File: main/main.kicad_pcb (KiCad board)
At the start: 2 copper layers, 28 parts, among them J1 Conn_01x10_Female, J2 USB_B, J3 AVR-ISP-6, J4 Micro_SD_Card, Q1 2N7002, Q2 BSS84, SW1 SW_Push, U1 ATmega1284P-PU, U2 AMS1117, U3 MCP2221A-I_SL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

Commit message: laid out pcb
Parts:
- added C8: 1u, Capacitor_SMD:C_1206_3216Metric, F.Cu at (101.2, 123.8)
- added C9: 1u, Capacitor_SMD:C_1206_3216Metric, F.Cu at (84.2, 123.2)
- U1: footprint Package_DIP:DIP-40_W15.24mm -> Package_QFP:TQFP-44_10x10mm_P0.8mm
- moved R6 96.3 mm to (81.4, 113.2), turned to 180 degrees
- moved J3 86.5 mm to (64.5, 86.0), turned to 90 degrees
- moved R7 84.5 mm to (84.2, 107.4), turned to 270 degrees
- moved U4 84.3 mm to (88.8, 90.0), turned to 180 degrees
- moved U2 81.3 mm to (89.8, 110.7), turned to 90 degrees
- moved J2 71.2 mm to (74.5, 120.8), turned to 180 degrees
- moved J4 70.1 mm to (66.8, 101.0), turned to 270 degrees
- moved R5 69.8 mm to (77.8, 95.0)
- moved C5 69.6 mm to (96.3, 107.5)
- moved R4 63.1 mm to (96.6, 85.8), turned to 180 degrees
- moved R3 62.6 mm to (103.1, 87.0)
- moved R8 60.0 mm to (81.0, 107.4), turned to 270 degrees
- moved U5 59.9 mm to (88.8, 98.9), turned to 180 degrees
- moved C7 57.8 mm to (80.8, 123.2), turned to 90 degrees
- moved U3 57.2 mm to (98.7, 115.7), turned to 180 degrees
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- renumbered SW1 to Reset
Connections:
- net Net-(J2-Pad2) renamed D-
- net Net-(J2-Pad3) renamed D+
- U4 pad 10: Net-(J3-Pad1) -> Net-(J3-Pad4)
- U4 pad 11: Net-(J3-Pad4) -> Net-(J3-Pad1)
- U4 pad 4: MOSI -> MISO
- U4 pad 5: MISO -> MOSI
- U5 pad 10: SD_MISO -> SD_MOSI
- U5 pad 11: SD_MOSI -> SD_MISO
- U5 pad 4: MOSI -> MISO
- U5 pad 5: MISO -> MOSI
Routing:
- net +3V3: track 0.00 -> 80.6 mm
- net RST: track 0.00 -> 75.9 mm
- net GND: track 0.00 -> 48.8 mm, vias 0 -> 17
- net SD_CS: track 0.00 -> 33.3 mm, vias 0 -> 3
- net Net-(J3-Pad1): track 0.00 -> 27.3 mm
- net Net-(Q2-Pad1): track 0.00 -> 26.5 mm
- net +5V: track 0.00 -> 24.7 mm, vias 0 -> 10
- net D+: track 0.00 -> 24.7 mm
- net SD_MOSI: track 0.00 -> 22.6 mm, vias 0 -> 2
- net Net-(J3-Pad4): track 0.00 -> 22.6 mm
- net SD_MISO: track 0.00 -> 22.5 mm, vias 0 -> 3
- net D-: track 0.00 -> 22.3 mm
- net CS: track 0.00 -> 22.1 mm, vias 0 -> 2
- net Net-(J3-Pad3): track 0.00 -> 21.7 mm
- net MOSI: track 0.00 -> 21.7 mm, vias 0 -> 2
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- added copper zone on VCC.Cu, net +5V
- added copper zone on GND.Cu, net GND
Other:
- board outline added: 70 x 57.5 mm
- copper layers 2 -> 4
- board text added: "3.3V ISP AVR"
- board text added: "Snug User Board V1"

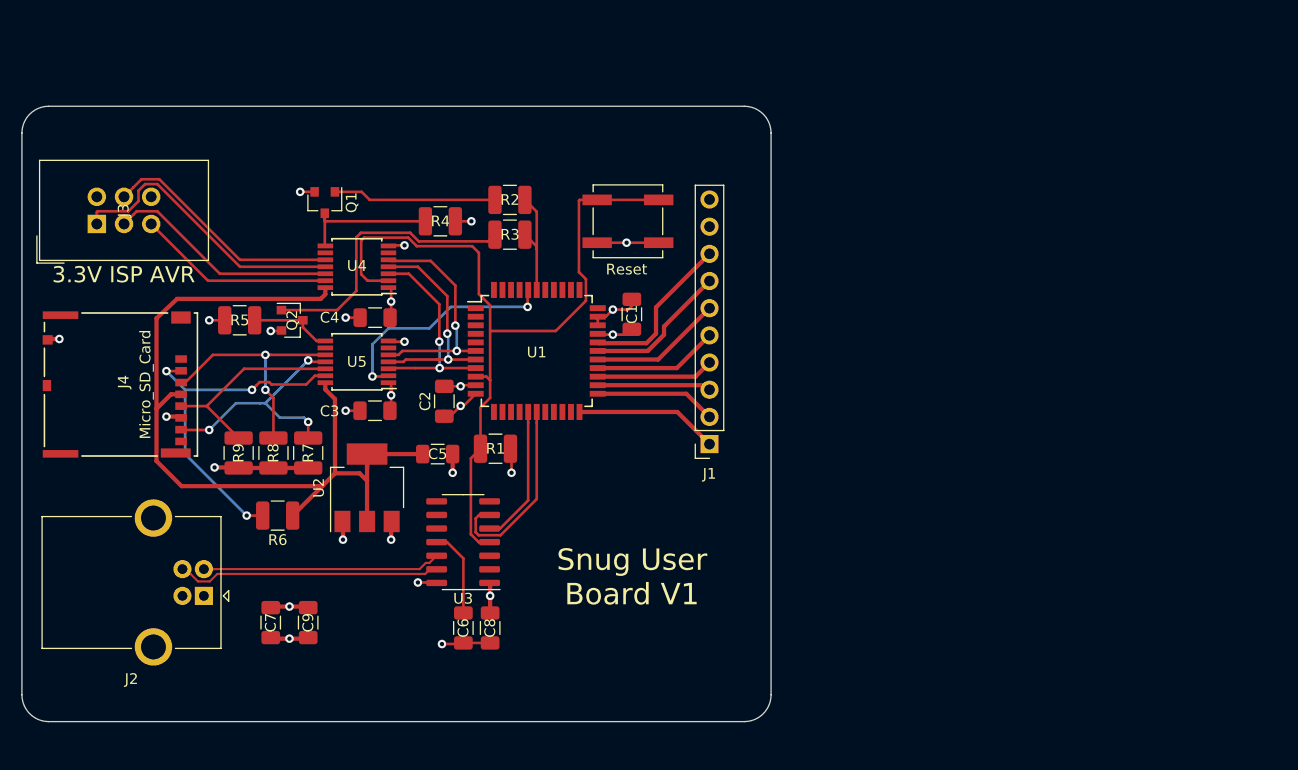
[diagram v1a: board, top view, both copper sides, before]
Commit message: added mounting holes
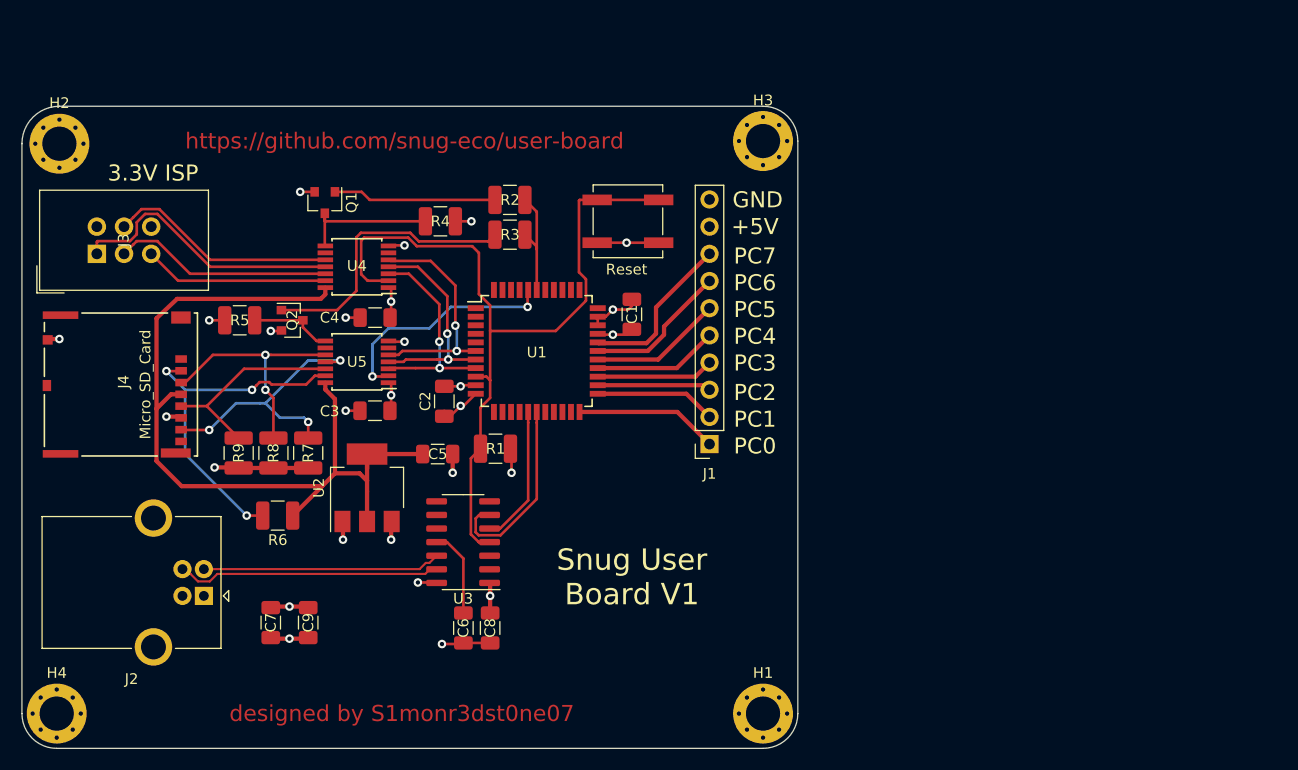
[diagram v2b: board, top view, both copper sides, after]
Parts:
- added H1: MountingHole_Pad, MountingHole:MountingHole_3.2mm_M3_DIN965_Pad, F.Cu at (126.8, 131.8)
- added H2: MountingHole_Pad, MountingHole:MountingHole_3.2mm_M3_DIN965_Pad, F.Cu at (61.0, 78.5)
- added H3: MountingHole_Pad, MountingHole:MountingHole_3.2mm_M3_DIN965_Pad, F.Cu at (126.8, 78.2)
- added H4: MountingHole_Pad, MountingHole:MountingHole_3.2mm_M3_DIN965_Pad, F.Cu at (60.8, 131.8)
- Reset: value SW_Push -> SW1
- moved J3 2.79 mm to (64.5, 88.8)
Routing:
- net SD_MISO: track 22.5 -> 25.3 mm
- net Net-(J3-Pad4): track 22.6 -> 21.5 mm
- net Net-(J3-Pad5): track 18.5 -> 17.3 mm
- net Net-(J3-Pad3): track 21.7 -> 20.6 mm
- net Net-(J3-Pad1): track 27.3 -> 26.3 mm
- net GND: vias 17 -> 49
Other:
- board size 70 x 57.5 mm -> 72.5 x 60 mm
- board text added: "+5V"
- board text added: "3.3V ISP"
- board text added: "GND"
- board text added: "PC0"
- board text added: "PC1"
- board text added: "PC2"
- board text added: "PC3"
- board text added: "PC4"
- board text added: "PC5"
- board text added: "PC6"
- board text added: "PC7"
- board text added: "designed by S1monr3dst0ne07"
- board text added: "https://github.com/snug-eco/user-board"
- board text removed: "3.3V ISP AVR"

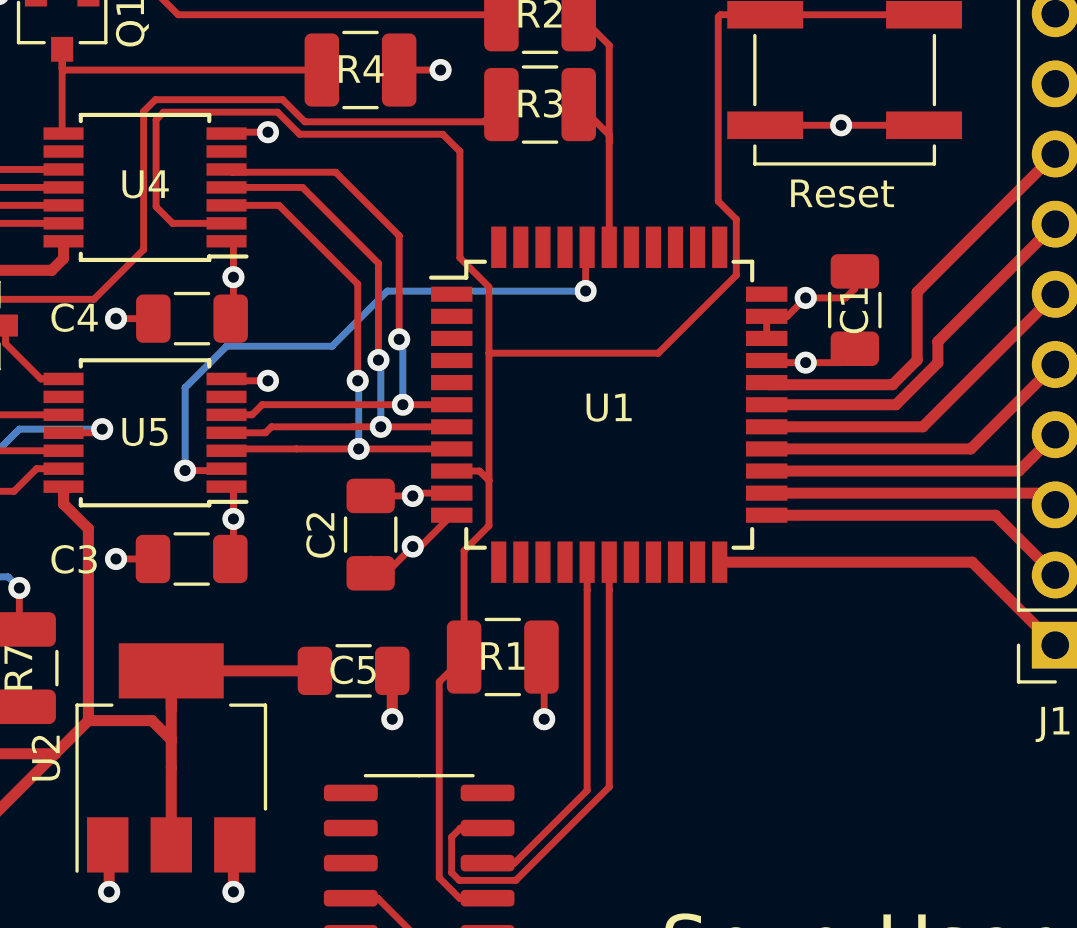
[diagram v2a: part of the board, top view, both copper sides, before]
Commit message: fixed 3.3v regulator cap
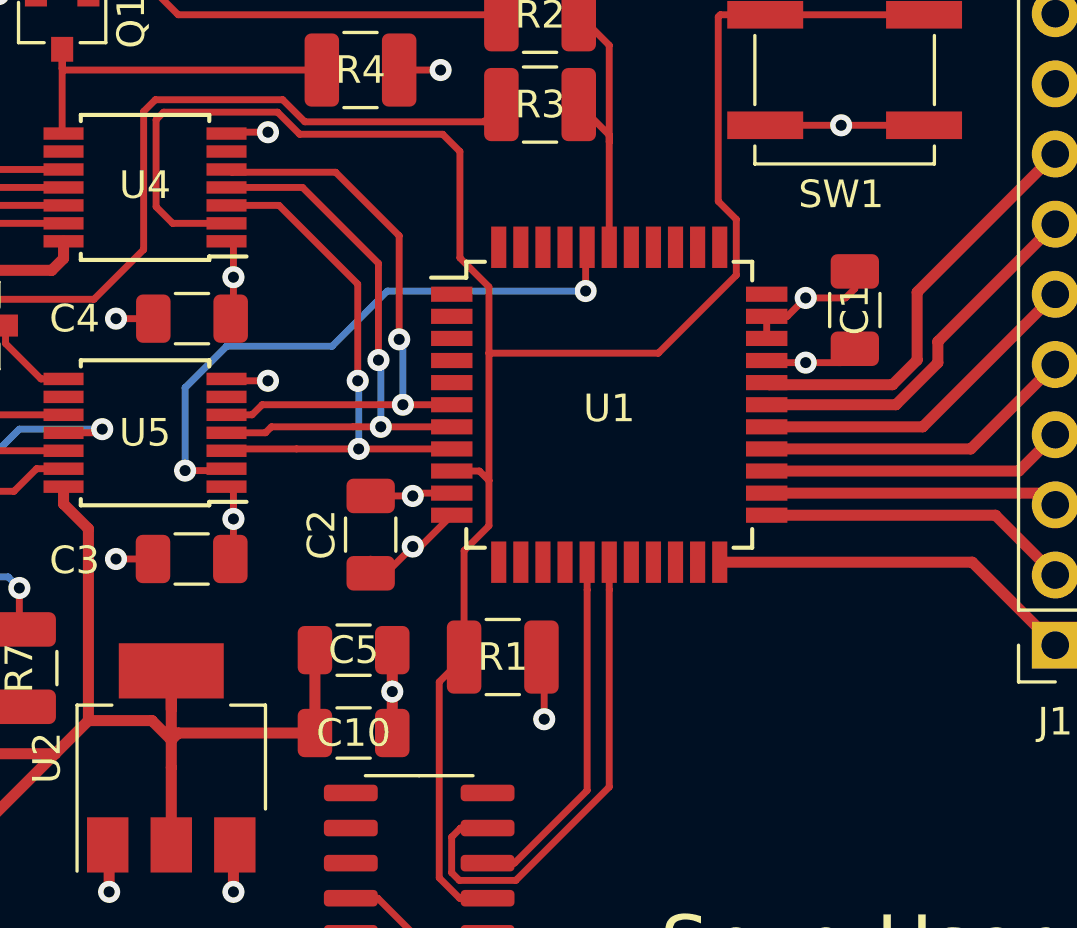
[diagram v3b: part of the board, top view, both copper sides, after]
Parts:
- added C10: 1u, Capacitor_SMD:C_1206_3216Metric, F.Cu at (96.3, 109.8)
- C5: value 1u -> 10u
- SW1: renamed from Reset; value SW1 -> Reset
- moved C5 0.75 mm to (96.3, 106.8)
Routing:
- net +3V3: track 80.6 -> 83.7 mm
- net GND: track 48.8 -> 50.1 mm
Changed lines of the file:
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@@
     (thickness 1.6)
     (drawings 22)
-    (tracks 376)
+    (tracks 379)
     (zones 0)
-    (modules 34)
+    (modules 35)
     (nets 67)
   )
@@
   )
   (setup
-    (last_trace_width 0.25)
+    (last_trace_width 0.4)
     (user_trace_width 0.25)
     (user_trace_width 0.4)
@@
     (add_net UTX)
   )
+  (module Capacitor_SMD:C_1206_3216Metric (layer F.Cu)
+    (at 96.35 109.75)
+    (descr "Capacitor SMD 1206 (3216 Metric), square (rectangular) end terminal, IPC_7351 nominal, (Body size source: http://www.tortai-tech.com/upload/download/2011102023233369053.pdf), generated with kicad-footprint-generator")
+    (tags capacitor)
+    (attr smd)
+    (fp_text reference C10 (at 0 0) (layer F.SilkS)
+      (effects (font (size 1 1) (thickness 0.15)))
+    )
+    (fp_text value 1u (at 0 1.82) (layer F.Fab)
+      (effects (font (size 1 1) (thickness 0.15)))
+    )
+    (fp_text user %R (at 0 0) (layer F.Fab)
+      (effects (font (size 0.8 0.8) (thickness 0.12)))
+    )
+    (fp_line (start 2.28 1.12) (end -2.28 1.12) (layer F.CrtYd) (width 0.05))
+    (fp_line (start 2.28 -1.12) (end 2.28 1.12) (layer F.CrtYd) (width 0.05))
+    (fp_line (start -2.28 -1.12) (end 2.28 -1.12) (layer F.CrtYd) (width 0.05))
+    (fp_line (start -2.28 1.12) (end -2.28 -1.12) (layer F.CrtYd) (width 0.05))
+    (fp_line (start -0.602064 0.91) (end 0.602064 0.91) (layer F.SilkS) (width 0.12))
+    (fp_line (start -0.602064 -0.91) (end 0.602064 -0.91) (layer F.SilkS) (width 0.12))
+    (fp_line (start 1.6 0.8) (end -1.6 0.8) (layer F.Fab) (width 0.1))
+    (fp_line (start 1.6 -0.8) (end 1.6 0.8) (layer F.Fab) (width 0.1))
+    (fp_line (start -1.6 -0.8) (end 1.6 -0.8) (layer F.Fab) (width 0.1))
+    (fp_line (start -1.6 0.8) (end -1.6 -0.8) (layer F.Fab) (width 0.1))
+    (pad 2 smd roundrect (at 1.4 0) (size 1.25 1.75) (layers F.Cu F.Paste F.Mask) (roundrect_rratio 0.2)
+      (net 1 GND))
+    (pad 1 smd roundrect (at -1.4 0) (size 1.25 1.75) (layers F.Cu F.Paste F.Mask) (roundrect_rratio 0.2)
+      (net 3 +3V3))
+    (model ${KISYS3DMOD}/Capacitor_SMD.3dshapes/C_1206_3216Metric.wrl
+      (at (xyz 0 0 0))
+      (scale (xyz 1 1 1))
+      (rotate (xyz 0 0 0))
+    )
+  )
   (module Connector_IDC:IDC-Header_2x03_P2.54mm_Vertical (layer F.Cu)
     (at 64.5 88.79 90)
@@
     (tags "Middle Stroke Tactile Switch")
     (attr smd)
-    (fp_text reference Reset (at -0.125 4.5) (layer F.SilkS)
-      (effects (font (size 1 1) (thickness 0.15)))
-    )
-    (fp_text value SW1 (at 0 4.75) (layer F.Fab)
+    (fp_text reference SW1 (at -0.125 4.5) (layer F.SilkS)
+      (effects (font (size 1 1) (thickness 0.15)))
+    )
+    (fp_text value Reset (at 0 4.75) (layer F.Fab)
       (effects (font (size 1 1) (thickness 0.15)))
     )
@@
   )
   (module Capacitor_SMD:C_1206_3216Metric (layer F.Cu)
-    (at 96.35 107.5)
+    (at 96.35 106.75)
     (descr "Capacitor SMD 1206 (3216 Metric), square (rectangular) end terminal, IPC_7351 nominal, (Body size source: http://www.tortai-tech.com/upload/download/2011102023233369053.pdf), generated with kicad-footprint-generator")
     (tags capacitor)
@@
       (effects (font (size 1 1) (thickness 0.15)))
     )
-    (fp_text value 1u (at 0 1.82) (layer F.Fab)
+    (fp_text value 10u (at 0 1.82) (layer F.Fab)
       (effects (font (size 1 1) (thickness 0.15)))
     )
@@
     (effects (font (size 1.5 1.5) (thickness 0.3)))
   )
-  (via (at 87.25 98.75) (size 0.8) (drill 0.4) (layers F.Cu B.Cu) (net 19))
   (via (at 59.25 130.25) (size 0.8) (drill 0.4) (layers F.Cu B.Cu) (net 1))
   (via (at 62.25 133.25) (size 0.8) (drill 0.4) (layers F.Cu B.Cu) (net 1))
@@
   (via (at 96.75 125.25) (size 0.8) (drill 0.4) (layers F.Cu B.Cu) (net 1))
   (via (at 87.5 115.5) (size 0.8) (drill 0.4) (layers F.Cu B.Cu) (net 1))
-  (via (at 97.75 109.25) (size 0.8) (drill 0.4) (layers F.Cu B.Cu) (net 1))
+  (via (at 97.75 108.25) (size 0.8) (drill 0.4) (layers F.Cu B.Cu) (net 1))
   (via (at 71 104) (size 0.8) (drill 0.4) (layers F.Cu B.Cu) (net 1))
   (via (at 61 96.75) (size 0.8) (drill 0.4) (layers F.Cu B.Cu) (net 1))
@@
   (segment (start 87.5 113.85) (end 87.45 113.8) (width 0.4) (layer F.Cu) (net 1))
   (segment (start 87.5 115.5) (end 87.5 113.85) (width 0.4) (layer F.Cu) (net 1))
-  (segment (start 97.75 107.5) (end 97.75 109.25) (width 0.4) (layer F.Cu) (net 1))
   (segment (start 98.65 125.25) (end 98.75 125.15) (width 0.25) (layer F.Cu) (net 1))
   (segment (start 96.75 125.25) (end 98.65 125.25) (width 0.25) (layer F.Cu) (net 1))
@@
   (segment (start 80.85 124.75) (end 80.75 124.65) (width 0.4) (layer F.Cu) (net 1))
   (segment (start 82.5 124.75) (end 80.85 124.75) (width 0.4) (layer F.Cu) (net 1))
+  (segment (start 97.75 108.25) (end 97.75 106.75) (width 0.4) (layer F.Cu) (net 1))
+  (segment (start 97.75 108.25) (end 97.75 109.75) (width 0.4) (layer F.Cu) (net 1))
   (via (at 82.5 121.75) (size 0.8) (drill 0.4) (layers F.Cu B.Cu) (net 2))
   (via (at 103.25 109.25) (size 0.8) (drill 0.4) (layers F.Cu B.Cu) (net 2))
@@
   (segment (start 86.75 102.357) (end 85.85 101.457) (width 0.4) (layer F.Cu) (net 3))
   (segment (start 86.75 109.3) (end 86.75 102.357) (width 0.4) (layer F.Cu) (net 3))
-  (segment (start 89.75 108.9) (end 89.75 107.5) (width 0.4) (layer F.Cu) (net 3))
-  (segment (start 94.95 107.5) (end 89.75 107.5) (width 0.4) (layer F.Cu) (net 3))
   (segment (start 89.75 113.8) (end 89.75 111) (width 0.4) (layer F.Cu) (net 3))
   (segment (start 86.75 109.3) (end 89.05 109.3) (width 0.4) (layer F.Cu) (net 3))
@@
   (segment (start 85.85 92.575) (end 85.425 93) (width 0.4) (layer F.Cu) (net 3))
   (segment (start 85.85 91.95) (end 85.85 92.575) (width 0.4) (layer F.Cu) (net 3))
+  (segment (start 94.95 106.75) (end 94.95 109.75) (width 0.4) (layer F.Cu) (net 3))
+  (segment (start 89.75 108.9) (end 89.75 107.5) (width 0.4) (layer F.Cu) (net 3))
+  (segment (start 90 109.75) (end 89.75 110) (width 0.4) (layer F.Cu) (net 3))
+  (segment (start 94.95 109.75) (end 90 109.75) (width 0.4) (layer F.Cu) (net 3))
   (segment (start 98.75 117.255) (end 97.225 115.73) (width 0.25) (layer F.Cu) (net 4))
   (segment (start 97.225 115.73) (end 96.25 115.73) (width 0.25) (layer F.Cu) (net 4))
@@
   (segment (start 69.009471 85.061399) (end 68.228601 85.842269) (width 0.25) (layer F.Cu) (net 17))
   (segment (start 85.85 90) (end 75.08913 90) (width 0.25) (layer F.Cu) (net 17))
+  (via (at 87.25 98.75) (size 0.8) (drill 0.4) (layers F.Cu B.Cu) (net 19))
   (via (at 84.25 104.5) (size 0.8) (drill 0.4) (layers F.Cu B.Cu) (net 19))
   (via (at 75 105.25) (size 0.8) (drill 0.4) (layers F.Cu B.Cu) (net 19))
